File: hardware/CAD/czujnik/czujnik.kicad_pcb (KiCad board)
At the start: 2 copper layers, 75 x 50 mm, 9 parts, among them J2 Barrel_Jack, J3 8P8C, U1 Pico

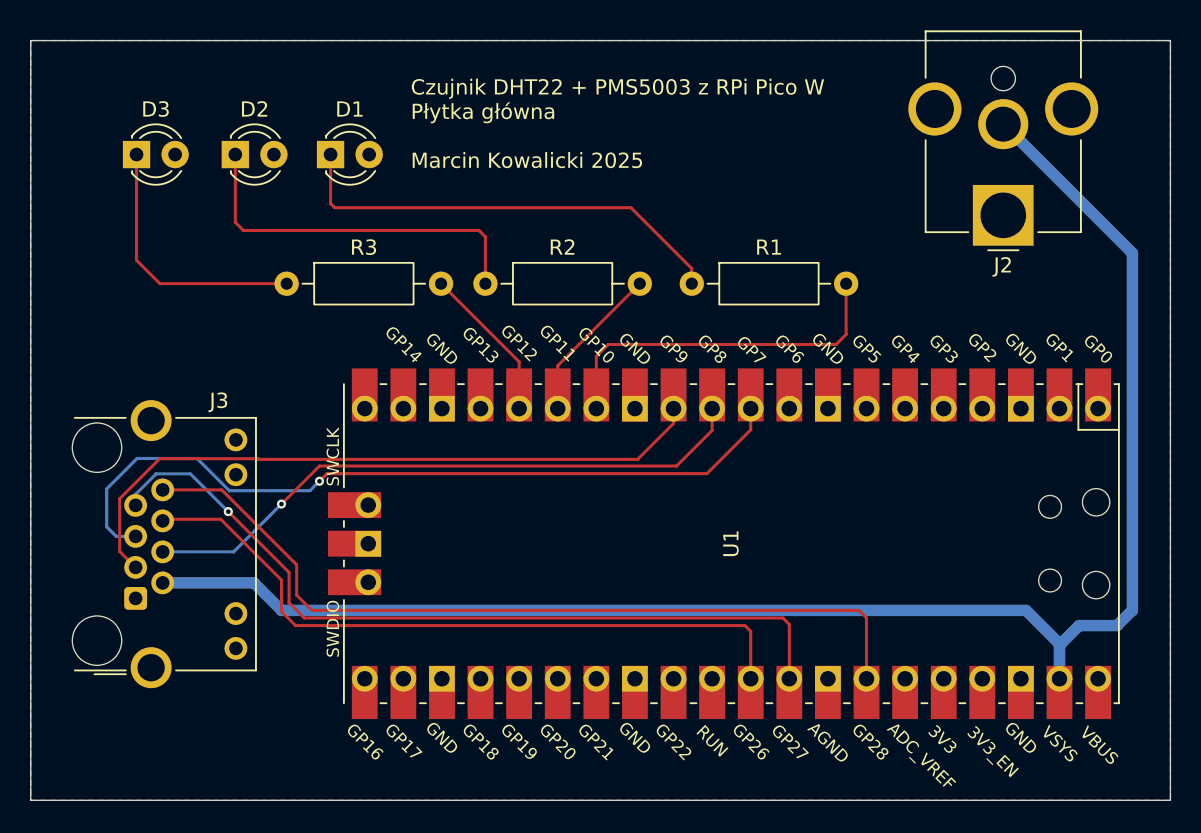
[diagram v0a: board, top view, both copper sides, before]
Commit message: refactor PCBs, add gerber files
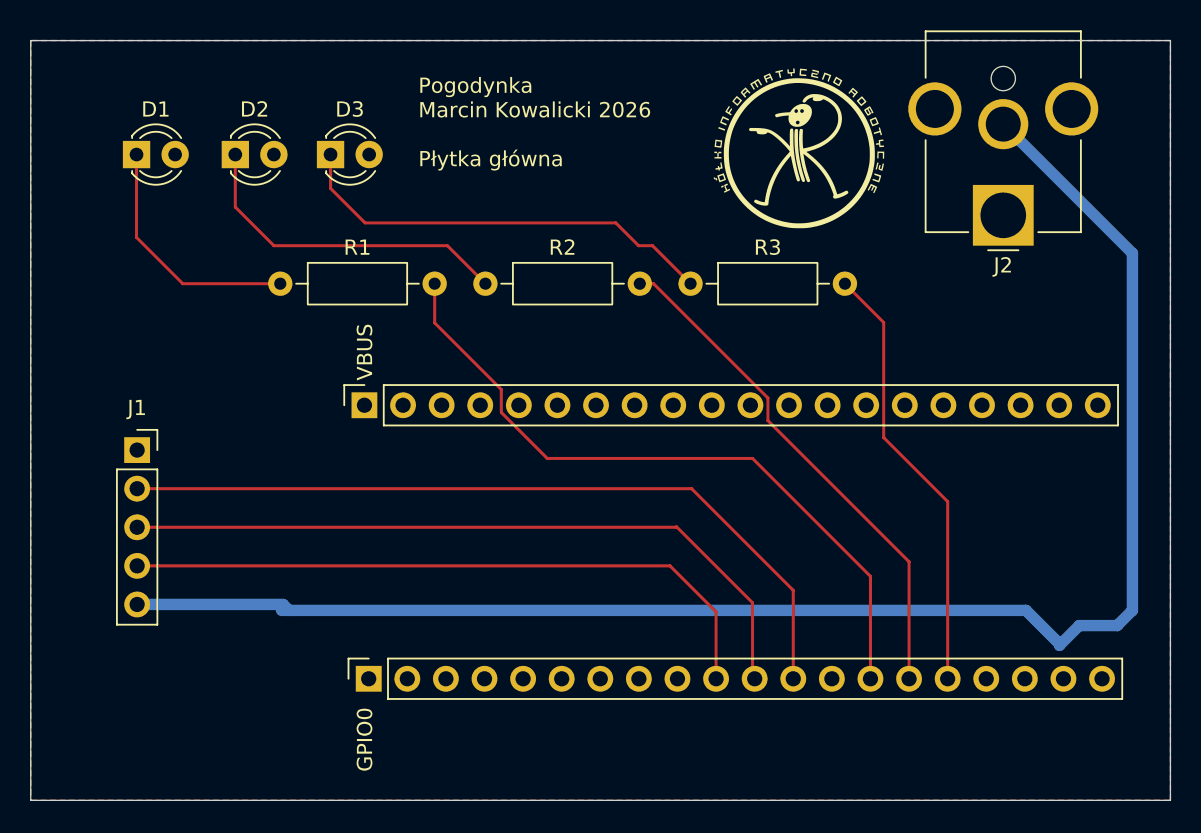
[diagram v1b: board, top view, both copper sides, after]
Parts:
- removed J3: 8P8C, Connector_RJ:RJ45_Connfly_DS1128-09-S8xx-S_Horizontal
- removed U1: Pico, MCU_RaspberryPi_and_Boards:RPi_Pico_SMD_TH
- added GPIO0: Conn_01x20_Socket, Connector_PinSocket_2.54mm:PinSocket_1x20_P2.54mm_Vertical, F.Cu at (135.7, 92.5)
- added J1: Conn_01x05_Socket, Connector_PinSocket_2.54mm:PinSocket_1x05_P2.54mm_Vertical, F.Cu at (120.5, 77.5)
- added VBUS: Conn_01x20_Socket, Connector_PinSocket_2.54mm:PinSocket_1x20_P2.54mm_Vertical, F.Cu at (135.5, 74.5)
- moved R1 27.1 mm to (129.9, 66.5)
- moved R3 26.6 mm to (156.9, 66.5)
- moved D1 12.8 mm to (120.5, 58.0)
- moved D3 12.8 mm to (133.2, 58.0)
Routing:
- net Net-(U1-GPIO28_ADC2): track 55.0 -> 0.00 mm
- net Net-(U1-GPIO27_ADC1): track 53.2 -> 0.00 mm, vias 1 -> 0
- net /DHT22: track 52.0 -> 0.00 mm, vias 1 -> 0
- net Net-(U1-GPIO26_ADC0): track 46.1 -> 0.00 mm
- net /DHT22_D: track 0.00 -> 43.8 mm
- net Net-(GPIO0-Pin_15): track 10.5 -> 33.9 mm
- net Net-(GPIO0-Pin_14): track 23.8 -> 45.8 mm
- net Net-(GPIO0-Pin_16): track 10.3 -> 28.8 mm
- net Net-(D1-K): track 29.8 -> 16.7 mm
- net Net-(D3-K): track 18.0 -> 28.5 mm
- net /TX: track 44.5 -> 51.8 mm
- net /RX: track 40.9 -> 47.6 mm, vias 1 -> 0
- net +5V: track 106.5 -> 103.6 mm
- net Net-(D2-K): track 24.4 -> 22.0 mm
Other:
- board text added: "Pogodynka Marcin Kowalicki 2026 Płytka główna"
- board text removed: "Czujnik DHT22 + PMS5003 z RPi Pico W Płytka główna Marcin Kowalicki 2025"

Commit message: add DB9 connectors to PCBs
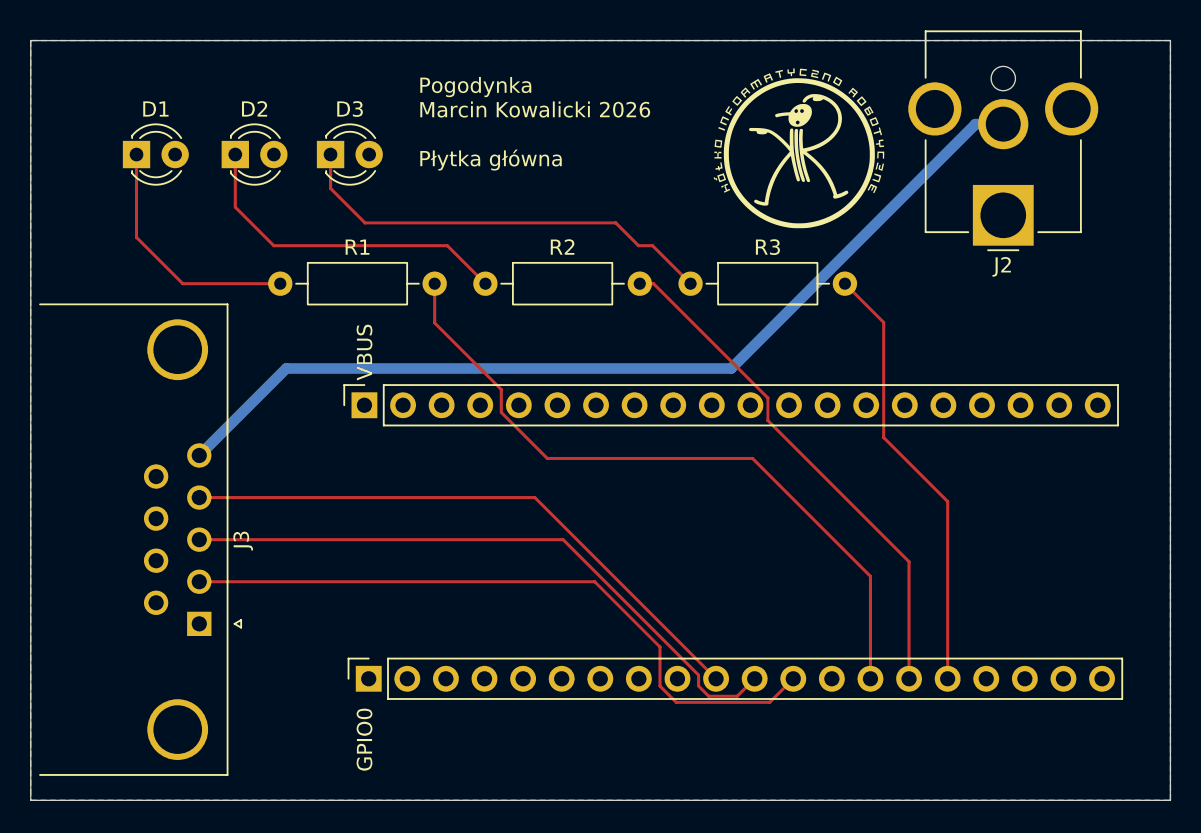
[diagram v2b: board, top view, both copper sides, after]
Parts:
- removed J1: Conn_01x05_Socket, Connector_PinSocket_2.54mm:PinSocket_1x05_P2.54mm_Vertical
- added J3: DE9_Socket, Connector_Dsub:DSUB-9_Socket_Horizontal_P2.77x2.84mm_EdgePinOffset7.70mm_Housed_MountingHolesOffset9.12mm, F.Cu at (124.6, 88.9)
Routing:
- net +5V: track 103.6 -> 61.9 mm
- net /TX: track 51.8 -> 44.5 mm
- net /RX: track 47.6 -> 41.7 mm
- net /DHT22_D: track 43.8 -> 38.9 mm

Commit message: add missing +5V path to rpi on main PCB
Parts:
- moved VBUS 48.4 mm to (183.8, 74.5), turned to -90 degrees
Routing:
- net +5V: track 61.9 -> 64.4 mm
